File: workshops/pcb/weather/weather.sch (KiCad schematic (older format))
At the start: 5 parts

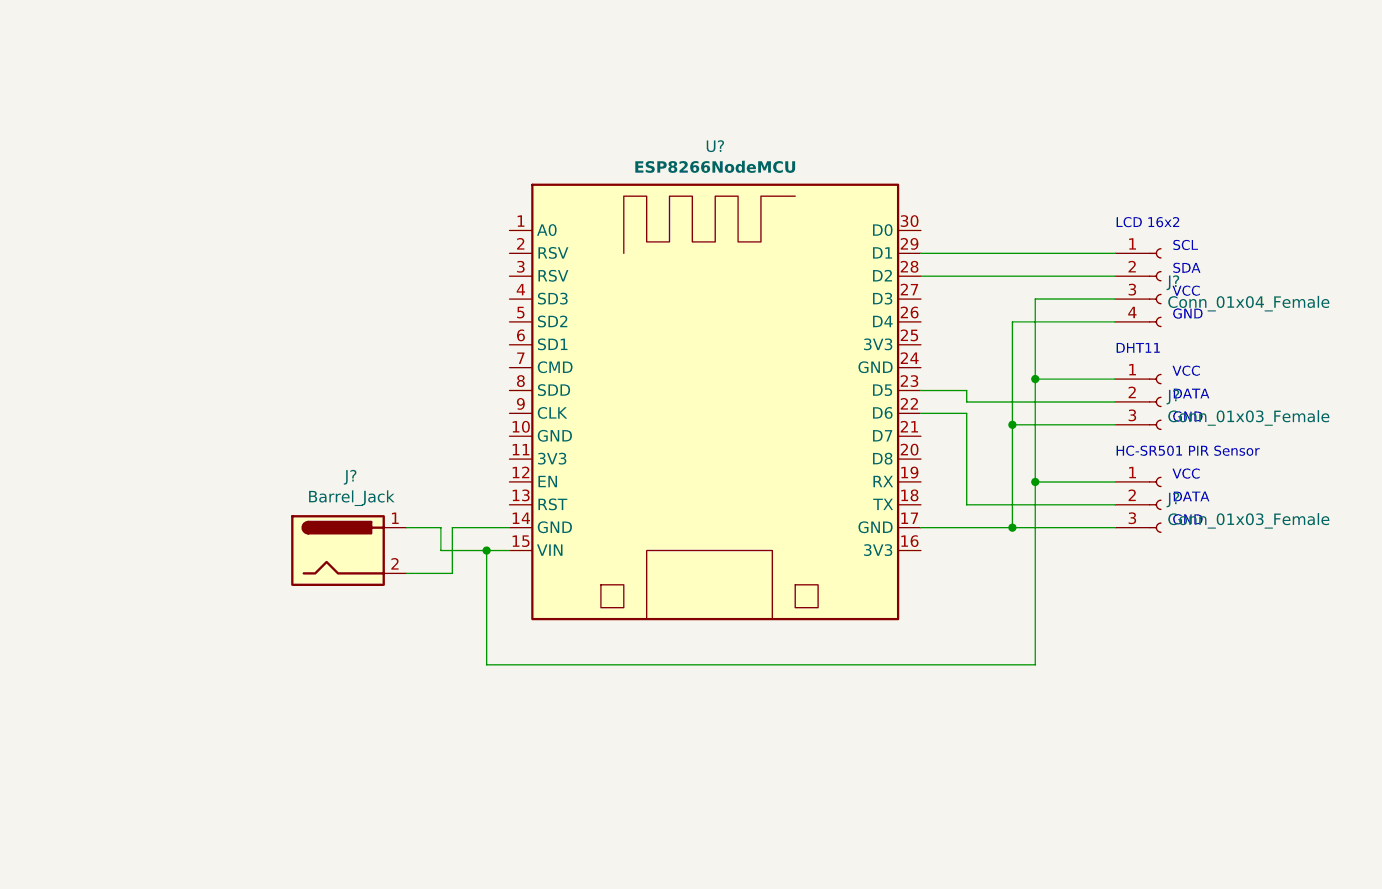
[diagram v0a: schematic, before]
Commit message: Update ESP8266_nodeMCU_V1.kicad_mod, MCU_Espressiv_8266nodemcu.lib, and 9 more files...
- Must add a 9v to 5v converters for sensors and LCD display that take 5v
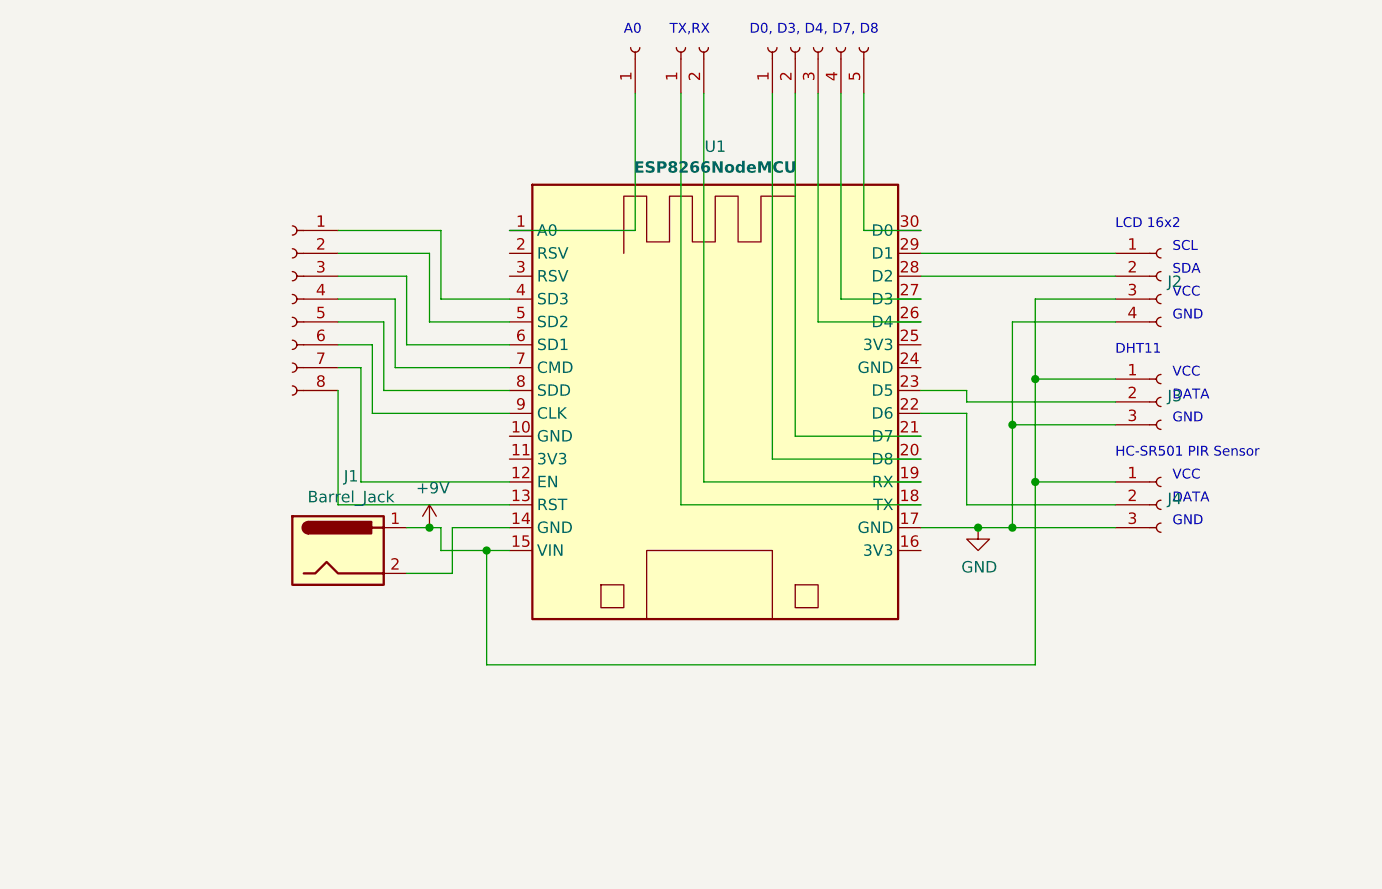
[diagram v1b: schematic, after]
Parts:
- added J5: Conn_01x08_Female, Connector_PinHeader_2.54mm:PinHeader_1x08_P2.54mm_Vertical, symbol Connector:Conn_01x08_Female
- added J6: Conn_01x01_Female, Connector_PinHeader_2.54mm:PinHeader_1x01_P2.54mm_Vertical, symbol Connector:Conn_01x01_Female
- added J7: Conn_01x02_Female, Connector_PinHeader_2.54mm:PinHeader_1x02_P2.54mm_Vertical, symbol Connector:Conn_01x02_Female
- added J8: Conn_01x05_Female, Connector_PinHeader_2.54mm:PinHeader_1x05_P2.54mm_Vertical, symbol Connector:Conn_01x05_Female
- J2: renamed from J?; footprint Connector_PinHeader_2.54mm:PinHeader_1x04_P2.54mm_Horizontal -> Connector_PinHeader_2.54mm:PinHeader_1x04_P2.54mm_Vertical
- J3, J4: renamed from J?; footprint Connector_PinHeader_2.54mm:PinHeader_1x03_P2.54mm_Horizontal -> Connector_PinHeader_2.54mm:PinHeader_1x03_P2.54mm_Vertical
- U1: renamed from U?; footprint smart_things_PCBv1:ESP8266_nodeMCU_V1 -> Module:ESP8266_nodeMCU_V1
- gave numbers to parts that had none: 1
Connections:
- net at U1.1 (A0): now also J6.1 (Pin_1)
- net at U1.12 (EN): now also J5.7 (Pin_7)
- net at U1.13 (RST): now also J5.8 (Pin_8)
- net +9V: now reaches J1.1, J2.3 (Pin_3), J3.1 (Pin_1), J4.1 (Pin_1), U1.15 (VIN)
- net GND: now reaches J2.4 (Pin_4), J3.3 (Pin_3), J4.3 (Pin_3), U1.17 (GND)
- net at U1.18 (TX): now also J7.1 (Pin_1)
- net at U1.19 (RX): now also J7.2 (Pin_2)
- net at U1.20 (D8): now also J8.1 (Pin_1)
- net at U1.21 (D7): now also J8.2 (Pin_2)
- net at U1.26 (D4): now also J8.3 (Pin_3)
- net at U1.27 (D3): now also J8.4 (Pin_4)
- net at U1.30 (D0): now also J8.5 (Pin_5)
- net at U1.4 (SD3): now also J5.1 (Pin_1)
- net at U1.5 (SD2): now also J5.2 (Pin_2)
- net at U1.6 (SD1): now also J5.3 (Pin_3)
- net at U1.7 (CMD): now also J5.4 (Pin_4)
- net at U1.8 (SDD): now also J5.5 (Pin_5)
- net at U1.9 (CLK): now also J5.6 (Pin_6)
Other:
- note added: "A0"
- note added: "D0, D3, D4, D7, D8"
- note added: "TX,RX"
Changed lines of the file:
@@
 encoding utf-8
 Sheet 1 1
-Title ""
-Date ""
-Rev ""
+Title "Smart Things - Home Weather Station"
+Date "2020-10-14"
+Rev "v1"
 Comp ""
 Comment1 ""
@@
 $EndDescr
 $Comp
-L MCU_Espressiv_8266nodemcu:ESP8266NodeMCU U?
+L MCU_Espressiv_8266nodemcu:ESP8266NodeMCU U1
 U 1 1 5F874528
 P 5250 3450
-F 0 "U?" H 5250 4517 50  0000 C CNN
+F 0 "U1" H 5250 4517 50  0000 C CNN
 F 1 "ESP8266NodeMCU" H 5250 4426 50  0000 C CNB
-F 2 "smart_things_PCBv1:ESP8266_nodeMCU_V1" H 5250 2150 50  0001 C CNN
+F 2 "Module:ESP8266_nodeMCU_V1" H 5250 2150 50  0001 C CNN
 F 3 "" H 5350 2150 50  0001 C CNN
 	1    5250 3450
@@
 $EndComp
 $Comp
-L Connector:Barrel_Jack J?
+L Connector:Barrel_Jack J1
 U 1 1 5F875BF7
 P 3600 4150
-F 0 "J?" H 3657 4475 50  0000 C CNN
+F 0 "J1" H 3657 4475 50  0000 C CNN
 F 1 "Barrel_Jack" H 3657 4384 50  0000 C CNN
 F 2 "Connector_BarrelJack:BarrelJack_Horizontal" H 3650 4110 50  0001 C CNN
@@
 $EndComp
 $Comp
-L Connector:Conn_01x04_Female J?
+L Connector:Conn_01x04_Female J2
 U 1 1 5F879B0C
 P 7200 2950
-F 0 "J?" H 7228 2926 50  0000 L CNN
-F 1 "Conn_01x04_Female" H 7228 2835 50  0000 L CNN
-F 2 "Connector_PinHeader_2.54mm:PinHeader_1x04_P2.54mm_Horizontal" H 7200 2950 50  0001 C CNN
+F 0 "J2" H 7228 2926 50  0000 L CNN
+F 1 "Conn_01x04_Female" H 7228 2835 50  0001 L CNN
+F 2 "Connector_PinHeader_2.54mm:PinHeader_1x04_P2.54mm_Vertical" H 7200 2950 50  0001 C CNN
 F 3 "~" H 7200 2950 50  0001 C CNN
 	1    7200 2950
@@
 $EndComp
 $Comp
-L Connector:Conn_01x03_Female J?
+L Connector:Conn_01x03_Female J4
 U 1 1 5F87805C
 P 7200 3950
-F 0 "J?" H 7228 3976 50  0000 L CNN
-F 1 "Conn_01x03_Female" H 7228 3885 50  0000 L CNN
-F 2 "Connector_PinHeader_2.54mm:PinHeader_1x03_P2.54mm_Horizontal" H 7200 3950 50  0001 C CNN
+F 0 "J4" H 7228 3976 50  0000 L CNN
+F 1 "Conn_01x03_Female" H 7228 3885 50  0001 L CNN
+F 2 "Connector_PinHeader_2.54mm:PinHeader_1x03_P2.54mm_Vertical" H 7200 3950 50  0001 C CNN
 F 3 "~" H 7200 3950 50  0001 C CNN
 	1    7200 3950
@@
 $EndComp
 $Comp
-L Connector:Conn_01x03_Female J?
+L Connector:Conn_01x03_Female J3
 U 1 1 5F876A09
 P 7200 3500
-F 0 "J?" H 7228 3526 50  0000 L CNN
-F 1 "Conn_01x03_Female" H 7228 3435 50  0000 L CNN
-F 2 "Connector_PinHeader_2.54mm:PinHeader_1x03_P2.54mm_Horizontal" H 7200 3500 50  0001 C CNN
+F 0 "J3" H 7228 3526 50  0000 L CNN
+F 1 "Conn_01x03_Female" H 7228 3435 50  0001 L CNN
+F 2 "Connector_PinHeader_2.54mm:PinHeader_1x03_P2.54mm_Vertical" H 7200 3500 50  0001 C CNN
 F 3 "~" H 7200 3500 50  0001 C CNN
 	1    7200 3500
@@
 DHT11\n
 Wire Wire Line
-	3900 4250 4100 4250
-Wire Wire Line
 	4100 4250 4100 4050
 Wire Wire Line
 	4100 4050 4350 4050
 Wire Wire Line
-	3900 4050 4050 4050
+	3900 4050 4000 4050
 Wire Wire Line
 	4050 4050 4050 4150
@@
 	4250 4150 4250 4650
 Wire Wire Line
-	4250 4650 6650 4650
-Wire Wire Line
 	6650 4650 6650 3850
 Wire Wire Line
@@
 	7000 4050 6550 4050
 Wire Wire Line
-	7000 3150 6550 3150
-Wire Wire Line
 	6550 3150 6550 3600
 Connection ~ 6550 4050
 Wire Wire Line
-	6550 4050 6150 4050
-Wire Wire Line
 	7000 3600 6550 3600
 Connection ~ 6550 3600
@@
 Wire Wire Line
 	6350 3550 6150 3550
+Wire Wire Line
+	4000 4050 4050 4050
+Wire Wire Line
+	6550 4050 6400 4050
+Wire Wire Line
+	7000 3150 6550 3150
+$Comp
+L power:GND #PWR0102
+U 1 1 5F8888C5
+P 6400 4050
+F 0 "#PWR0102" H 6400 3800 50  0001 C CNN
+F 1 "GND" H 6405 3877 50  0000 C CNN
+F 2 "" H 6400 4050 50  0001 C CNN
+F 3 "" H 6400 4050 50  0001 C CNN
+	1    6400 4050
+	1    0    0    -1
+$EndComp
+Connection ~ 6400 4050
+Wire Wire Line
+	6400 4050 6150 4050
+$Comp
+L power:+9V #PWR0101
+U 1 1 5F885573
+P 4000 4050
+F 0 "#PWR0101" H 4000 3900 50  0001 C CNN
+F 1 "+9V" H 4015 4223 50  0000 C CNN
+F 2 "" H 4000 4050 50  0001 C CNN
+F 3 "" H 4000 4050 50  0001 C CNN
+	1    4000 4050
+	1    0    0    -1
+$EndComp
+Connection ~ 4000 4050
+Wire Wire Line
+	4250 4650 6650 4650
+Wire Wire Line
+	3900 4250 4100 4250
+$Comp
+L Connector:Conn_01x05_Female J8
+U 1 1 5F882423
+P 5700 1950
+F 0 "J8" V 5592 1662 50  0001 R CNN
+F 1 "Conn_01x05_Female" V 5547 1662 50  0001 R CNN
+F 2 "Connector_PinHeader_2.54mm:PinHeader_1x05_P2.54mm_Vertical" H 5700 1950 50  0001 C CNN
+F 3 "~" H 5700 1950 50  0001 C CNN
+	1    5700 1950
+	0    -1   -1   0
+$EndComp
+Text Notes 5400 1900 0    43   ~ 0
+D0, D3, D4, D7, D8
+Wire Wire Line
+	6150 2750 5900 2750
+Wire Wire Line
+	5900 2750 5900 2150
+Wire Wire Line
+	6150 3050 5800 3050
+Wire Wire Line
+	5800 3050 5800 2150
+Wire Wire Line
+	6150 3150 5700 3150
+Wire Wire Line
+	5700 3150 5700 2150
+Wire Wire Line
+	6150 3650 5600 3650
+Wire Wire Line
+	5600 3650 5600 2150
+Wire Wire Line
+	6150 3750 5500 3750
+Wire Wire Line
+	5500 3750 5500 2150
+$Comp
+L Connector:Conn_01x02_Female J7
+U 1 1 5F889B2E
+P 5100 1950
+F 0 "J7" V 4992 1762 50  0001 R CNN
+F 1 "Conn_01x02_Female" V 4947 1762 50  0001 R CNN
+F 2 "Connector_PinHeader_2.54mm:PinHeader_1x02_P2.54mm_Vertical" H 5100 1950 50  0001 C CNN
+F 3 "~" H 5100 1950 50  0001 C CNN
+	1    5100 1950
+	0    -1   -1   0
+$EndComp
+Text Notes 5050 1900 0    43   ~ 0
+TX,RX
+Wire Wire Line
+	6150 3850 5200 3850
+Wire Wire Line
+	5200 3850 5200 2150
+Wire Wire Line
+	6150 3950 5100 3950
+Wire Wire Line
+	5100 3950 5100 2150
+$Comp
+L Connector:Conn_01x01_Female J6
+U 1 1 5F88DFE0
+P 4900 1950
+F 0 "J6" V 4838 1862 50  0001 R CNN
+F 1 "Conn_01x01_Female" V 4792 1862 50  0001 R CNN
+F 2 "Connector_PinHeader_2.54mm:PinHeader_1x01_P2.54mm_Vertical" H 4900 1950 50  0001 C CNN
+F 3 "~" H 4900 1950 50  0001 C CNN
+	1    4900 1950
+	0    -1   -1   0
+$EndComp
+Text Notes 4850 1900 0    43   ~ 0
+A0
+Wire Wire Line
+	4900 2150 4900 2750
+Wire Wire Line
+	4900 2750 4350 2750
+$Comp
+L Connector:Conn_01x08_Female J5
+U 1 1 5F890933
+P 3400 3050
+F 0 "J5" H 3292 3443 50  0001 C CNN
+F 1 "Conn_01x08_Female" H 3292 3444 50  0001 C CNN
+F 2 "Connector_PinHeader_2.54mm:PinHeader_1x08_P2.54mm_Vertical" H 3400 3050 50  0001 C CNN
+F 3 "~" H 3400 3050 50  0001 C CNN
+	1    3400 3050
+	-1   0    0    -1
+$EndComp
+Wire Wire Line
+	4350 3950 3600 3950
+Wire Wire Line
+	3600 3950 3600 3450
+Wire Wire Line
+	4350 3850 3700 3850
+Wire Wire Line
+	3700 3850 3700 3350
+Wire Wire Line
+	3700 3350 3600 3350
+Wire Wire Line
+	4350 3550 3750 3550
+Wire Wire Line
+	3750 3550 3750 3250
+Wire Wire Line
+	3750 3250 3600 3250
+Wire Wire Line
+	4350 3450 3800 3450
+Wire Wire Line
+	3800 3450 3800 3150
+Wire Wire Line
+	3800 3150 3600 3150
+Wire Wire Line
+	4350 3350 3850 3350
+Wire Wire Line
+	3850 3350 3850 3050
+Wire Wire Line
+	3850 3050 3600 3050
+Wire Wire Line
+	4350 3250 3900 3250
+Wire Wire Line
+	3900 3250 3900 2950
+Wire Wire Line
+	3900 2950 3600 2950
+Wire Wire Line
+	4350 3150 4000 3150
+Wire Wire Line
+	4000 3150 4000 2850
+Wire Wire Line
+	4000 2850 3600 2850
+Wire Wire Line
+	4350 3050 4050 3050
+Wire Wire Line
+	4050 3050 4050 2750
+Wire Wire Line
+	4050 2750 3600 2750
 $EndSCHEMATC

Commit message: Update custom_logo.kicad_mod, fp-info-cache, and 7 more files...
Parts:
- added J10, J11, J9: Conn_01x03_Female, Connector_PinHeader_2.54mm:PinHeader_1x03_P2.54mm_Vertical, symbol Connector:Conn_01x03_Female
- added J12: Conn_01x06_Female, Connector_PinHeader_2.54mm:PinHeader_1x06_P2.54mm_Vertical, symbol Connector:Conn_01x06_Female
- added R1: 1.2K ohm, Resistor_THT:R_Axial_DIN0309_L9.0mm_D3.2mm_P12.70mm_Horizontal, symbol Device:R
- added R2: 1.5K ohm, Resistor_THT:R_Axial_DIN0309_L9.0mm_D3.2mm_P12.70mm_Horizontal, symbol Device:R
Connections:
- net +9V: now also J9.1 (Pin_1), J9.2 (Pin_2), J9.3 (Pin_3), R1.1; no longer J2.3 (Pin_3), J3.1 (Pin_1), J4.1 (Pin_1)
- net GND: now also J1.2, U1.10 (GND), U1.14 (GND), J12.1 (Pin_1), J12.2 (Pin_2), J12.3 (Pin_3), J12.4 (Pin_4), J12.5 (Pin_5), J12.6 (Pin_6), R2.2
- net +3V3: now reaches U1.11 (3V3)
- net +3V3: now also J11.1 (Pin_1), J11.2 (Pin_2), J11.3 (Pin_3)
- new net +5V: J10.1 (Pin_1), J10.2 (Pin_2), J10.3 (Pin_3), J2.3 (Pin_3), J3.1 (Pin_1), J4.1 (Pin_1), R1.2, R2.1
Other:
- note added: "3V3"
- note added: "5V"
- note added: "9V"
- moved on the sheet: J1
